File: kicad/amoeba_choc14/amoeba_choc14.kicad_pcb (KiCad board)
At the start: 2 copper layers, 13.7 x 16 mm, 8 parts, among them J1 Conn_01x01_Pin, J2 Conn_01x01_Pin, J3 Conn_01x01_Pin, J4 Conn_01x01_Pin, SW1 SW_SPST

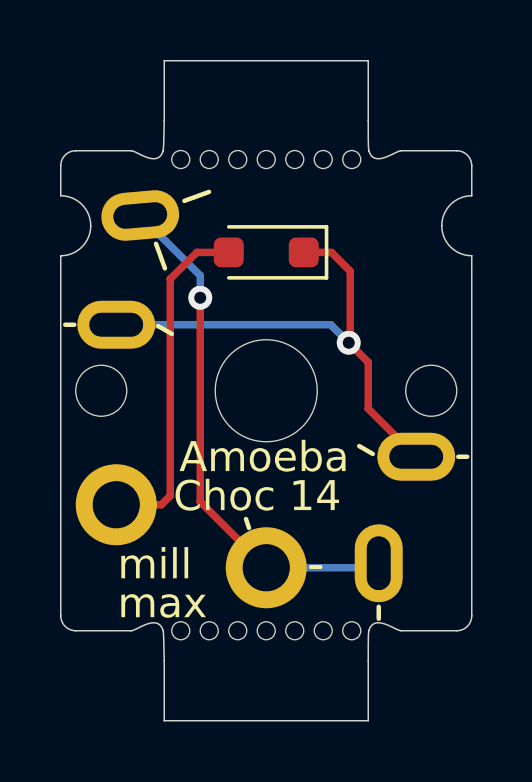
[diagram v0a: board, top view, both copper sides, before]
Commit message: feat(amoeba): bump version, straighten trace
-   update to KiCad 9
-   increase font size in schematic
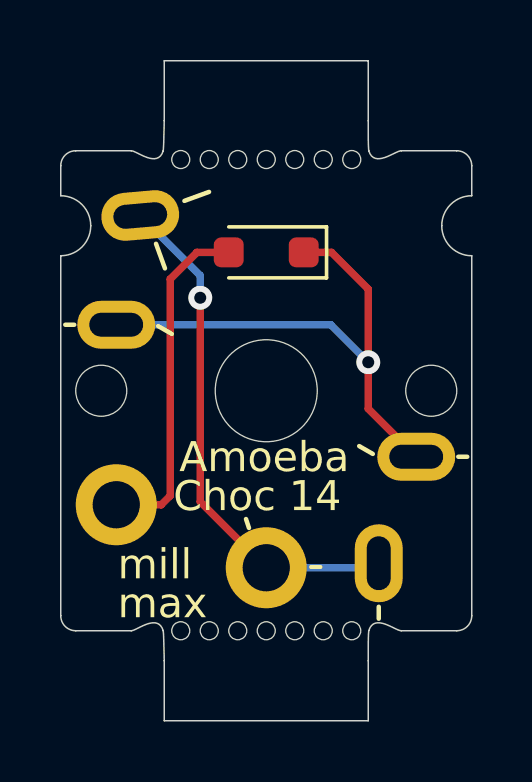
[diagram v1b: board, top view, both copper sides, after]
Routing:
- net /row: track 16.7 -> 17.6 mm
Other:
- board text added: "Outer ticks: choc spacing - 18 w x 17 h Inner ticks: clip width x body length - 14.5 w x 13.8 h Blue outline: switch lower body - 13.8 w x 13.8 h"
- board text added: "v010a3"
- board text removed: "Outer ticks: choc spacing - 18 x 17 Inner ticks: clip width x body length - 14.5 x 13.8 Blue outline: switch lower body - 13.8 x 13.8"
- board text removed: "v010a2"

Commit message: feat(amoeba): SOD-123 diode, fewer silk tick marks
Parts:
- D1: footprint Diode_SMD:D_SOD-323_HandSoldering -> Diode_SMD:D_SOD-123
- moved D1 0.09 mm to (130.0, 105.3)
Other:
- board text added: "v010a4"
- board text removed: "v010a3"
